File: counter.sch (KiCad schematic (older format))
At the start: 5 parts

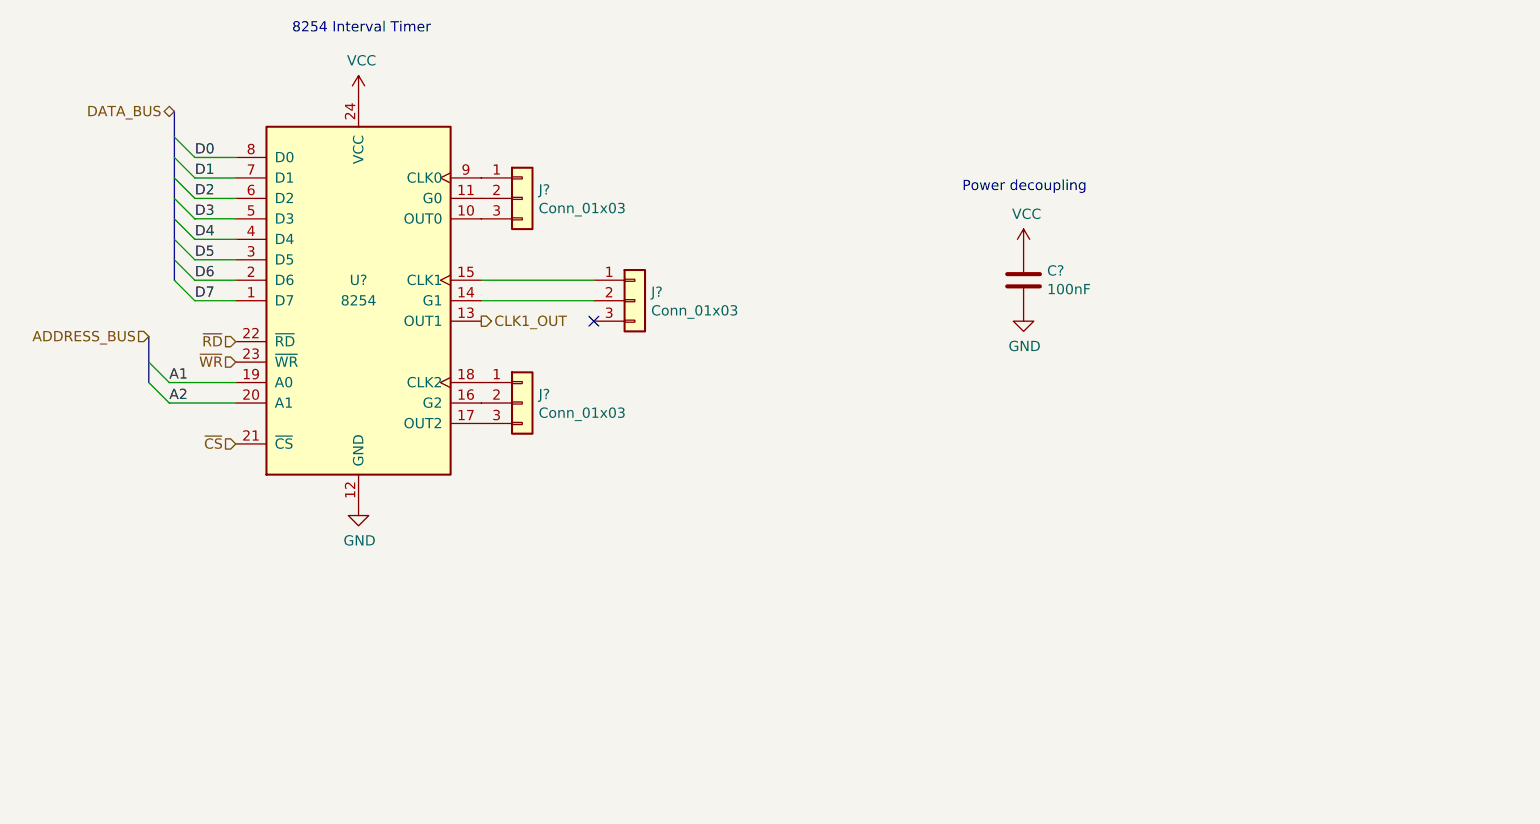
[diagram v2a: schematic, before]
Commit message: General edits; removed floating inputs
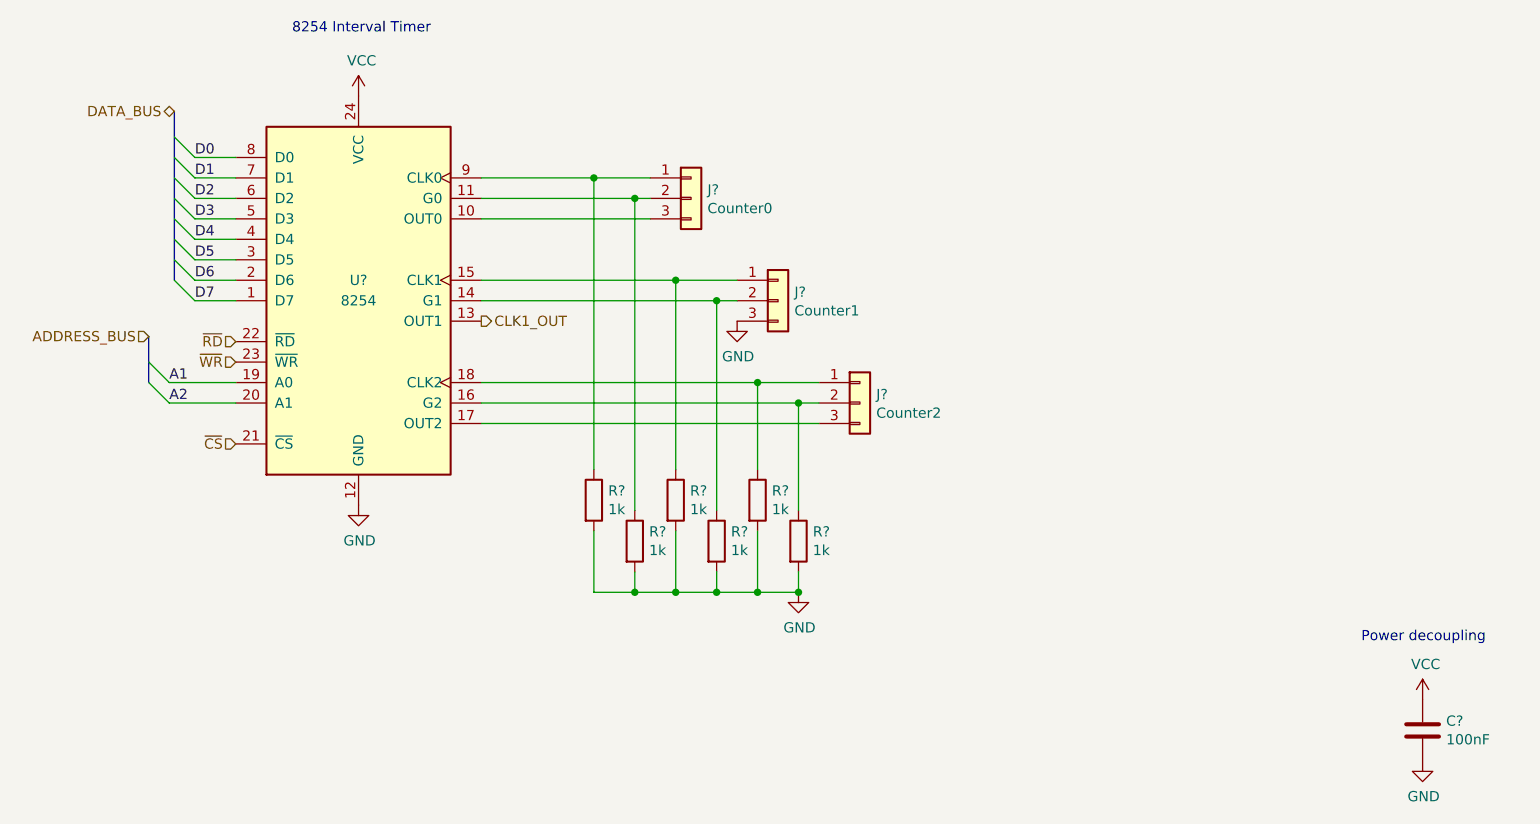
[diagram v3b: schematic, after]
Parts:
- added R? (x6): 1k, symbol Device:R
- J?: value Conn_01x03 -> Counter0
- J?: value Conn_01x03 -> Counter1
- J?: value Conn_01x03 -> Counter2
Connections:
- net GND: now also J?.3 (Pin_3), R?.2, R?.2, R?.2, R?.2, R?.2, R?.2
- net at J?.2 (Pin_2), U?.11 (G0): now also R?.1
- net at J?.2 (Pin_2), U?.14 (G1): now also R?.1
- net at J?.1 (Pin_1), U?.15 (CLK1): now also R?.1
- net at J?.2 (Pin_2), U?.16 (G2): now also R?.1
- net at J?.1 (Pin_1), U?.18 (CLK2): now also R?.1
- net at J?.1 (Pin_1), U?.9 (CLK0): now also R?.1
- no-connect marks 1 -> 0
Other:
- moved on the sheet: C?, J?

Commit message: Updates to pass ERC
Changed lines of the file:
@@
 D7
 Text HLabel 4100 2800 0    50   BiDi ~ 0
-DATA_BUS
+D[0..15]
 Text HLabel 4400 3925 0    50   Input ~ 0
 ~RD
@@
 	3975 4125 4075 4225
 Text HLabel 3975 3900 0    50   Input ~ 0
-ADDRESS_BUS
+A[0..19]
 Text HLabel 4400 4425 0    50   Input ~ 0
 ~CS
@@
 Wire Wire Line
 	6150 5150 6350 5150
-Wire Bus Line
-	3975 3900 3975 4125
-Wire Bus Line
-	4100 2800 4100 3625
 Connection ~ 6350 5150
 $Comp
@@
 	1    0    0    -1
 $EndComp
+Wire Bus Line
+	3975 3900 3975 4125
+Wire Bus Line
+	4100 2800 4100 3625
 $EndSCHEMATC

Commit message: Assign footprints for most symbols
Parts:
- C20: renamed from C?; footprint (none) -> Capacitor_THT:C_Rect_L4.0mm_W2.5mm_P2.50mm
- J17, J18, J19: renamed from J?; footprint (none) -> Connector_PinHeader_2.54mm:PinHeader_1x03_P2.54mm_Vertical
- R12, R13, R14, R15, R16, R17: renamed from R?; footprint (none) -> Resistor_THT:R_Axial_DIN0207_L6.3mm_D2.5mm_P10.16mm_Horizontal
- gave numbers to parts that had none: 1
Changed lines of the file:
@@
 $EndDescr
 $Comp
-L Timer:8254 U?
+L Timer:8254 U17
 U 1 1 61CE17BA
 P 5000 3725
-F 0 "U?" H 5000 3825 50  0000 C CNN
+F 0 "U17" H 5000 3825 50  0000 C CNN
 F 1 "8254" H 5000 3725 50  0000 C CNN
 F 2 "Package_DIP:DIP-24_W15.24mm" H 5050 3975 50  0001 C CNN
@@
 ~CS
 $Comp
-L Connector_Generic:Conn_01x03 J?
+L Connector_Generic:Conn_01x03 J17
 U 1 1 61CE9805
 P 6625 3225
-F 0 "J?" H 6705 3267 50  0000 L CNN
+F 0 "J17" H 6705 3267 50  0000 L CNN
 F 1 "Counter0" H 6705 3176 50  0000 L CNN
-F 2 "" H 6625 3225 50  0001 C CNN
+F 2 "Connector_PinHeader_2.54mm:PinHeader_1x03_P2.54mm_Vertical" H 6625 3225 50  0001 C CNN
 F 3 "~" H 6625 3225 50  0001 C CNN
 	1    6625 3225
@@
 $EndComp
 $Comp
-L Connector_Generic:Conn_01x03 J?
+L Connector_Generic:Conn_01x03 J18
 U 1 1 61CE9E55
 P 7050 3725
-F 0 "J?" H 7130 3767 50  0000 L CNN
+F 0 "J18" H 7130 3767 50  0000 L CNN
 F 1 "Counter1" H 7130 3676 50  0000 L CNN
-F 2 "" H 7050 3725 50  0001 C CNN
+F 2 "Connector_PinHeader_2.54mm:PinHeader_1x03_P2.54mm_Vertical" H 7050 3725 50  0001 C CNN
 F 3 "~" H 7050 3725 50  0001 C CNN
 	1    7050 3725
@@
 $EndComp
 $Comp
-L Connector_Generic:Conn_01x03 J?
+L Connector_Generic:Conn_01x03 J19
 U 1 1 61CEA43A
 P 7450 4225
-F 0 "J?" H 7530 4267 50  0000 L CNN
+F 0 "J19" H 7530 4267 50  0000 L CNN
 F 1 "Counter2" H 7530 4176 50  0000 L CNN
-F 2 "" H 7450 4225 50  0001 C CNN
+F 2 "Connector_PinHeader_2.54mm:PinHeader_1x03_P2.54mm_Vertical" H 7450 4225 50  0001 C CNN
 F 3 "~" H 7450 4225 50  0001 C CNN
 	1    7450 4225
@@
 CLK1_OUT
 $Comp
-L power:VCC #PWR?
+L power:VCC #PWR0170
 U 1 1 61CEF955
 P 5000 2725
-F 0 "#PWR?" H 5000 2575 50  0001 C CNN
+F 0 "#PWR0170" H 5000 2575 50  0001 C CNN
 F 1 "VCC" H 5015 2898 50  0000 C CNN
 F 2 "" H 5000 2725 50  0001 C CNN
@@
 $EndComp
 $Comp
-L power:GND #PWR?
+L power:GND #PWR0171
 U 1 1 61CEFD63
 P 5000 4725
-F 0 "#PWR?" H 5000 4475 50  0001 C CNN
+F 0 "#PWR0171" H 5000 4475 50  0001 C CNN
 F 1 "GND" H 5005 4552 50  0000 C CNN
 F 2 "" H 5000 4725 50  0001 C CNN
@@
 $EndComp
 $Comp
-L Device:C C?
+L Device:C C20
 U 1 1 61CF103C
 P 10200 5825
-F 0 "C?" H 10315 5871 50  0000 L CNN
+F 0 "C20" H 10315 5871 50  0000 L CNN
 F 1 "100nF" H 10315 5780 50  0000 L CNN
-F 2 "" H 10238 5675 50  0001 C CNN
+F 2 "Capacitor_THT:C_Rect_L4.0mm_W2.5mm_P2.50mm" H 10238 5675 50  0001 C CNN
 F 3 "~" H 10200 5825 50  0001 C CNN
 	1    10200 5825
@@
 $EndComp
 $Comp
-L power:VCC #PWR?
+L power:VCC #PWR0172
 U 1 1 61CF1476
 P 10200 5675
-F 0 "#PWR?" H 10200 5525 50  0001 C CNN
+F 0 "#PWR0172" H 10200 5525 50  0001 C CNN
 F 1 "VCC" H 10215 5848 50  0000 C CNN
 F 2 "" H 10200 5675 50  0001 C CNN
@@
 $EndComp
 $Comp
-L power:GND #PWR?
+L power:GND #PWR0173
 U 1 1 61CF1948
 P 10200 5975
-F 0 "#PWR?" H 10200 5725 50  0001 C CNN
+F 0 "#PWR0173" H 10200 5725 50  0001 C CNN
 F 1 "GND" H 10205 5802 50  0000 C CNN
 F 2 "" H 10200 5975 50  0001 C CNN
@@
 	5600 4325 7250 4325
 $Comp
-L Device:R R?
+L Device:R R12
 U 1 1 622F8E00
 P 6150 4700
-F 0 "R?" H 6220 4746 50  0000 L CNN
+F 0 "R12" H 6220 4746 50  0000 L CNN
 F 1 "1k" H 6220 4655 50  0000 L CNN
-F 2 "" V 6080 4700 50  0001 C CNN
+F 2 "Resistor_THT:R_Axial_DIN0207_L6.3mm_D2.5mm_P10.16mm_Horizontal" V 6080 4700 50  0001 C CNN
 F 3 "~" H 6150 4700 50  0001 C CNN
 	1    6150 4700
@@
 $EndComp
 $Comp
-L Device:R R?
+L Device:R R13
 U 1 1 622FACCC
 P 6350 4900
-F 0 "R?" H 6420 4946 50  0000 L CNN
+F 0 "R13" H 6420 4946 50  0000 L CNN
 F 1 "1k" H 6420 4855 50  0000 L CNN
-F 2 "" V 6280 4900 50  0001 C CNN
+F 2 "Resistor_THT:R_Axial_DIN0207_L6.3mm_D2.5mm_P10.16mm_Horizontal" V 6280 4900 50  0001 C CNN
 F 3 "~" H 6350 4900 50  0001 C CNN
 	1    6350 4900
@@
 $EndComp
 $Comp
-L Device:R R?
+L Device:R R14
 U 1 1 622FBCA0
 P 6550 4700
-F 0 "R?" H 6620 4746 50  0000 L CNN
+F 0 "R14" H 6620 4746 50  0000 L CNN
 F 1 "1k" H 6620 4655 50  0000 L CNN
-F 2 "" V 6480 4700 50  0001 C CNN
+F 2 "Resistor_THT:R_Axial_DIN0207_L6.3mm_D2.5mm_P10.16mm_Horizontal" V 6480 4700 50  0001 C CNN
 F 3 "~" H 6550 4700 50  0001 C CNN
 	1    6550 4700
@@
 $EndComp
 $Comp
-L Device:R R?
+L Device:R R15
 U 1 1 622FC929
 P 6750 4900
-F 0 "R?" H 6820 4946 50  0000 L CNN
+F 0 "R15" H 6820 4946 50  0000 L CNN
 F 1 "1k" H 6820 4855 50  0000 L CNN
-F 2 "" V 6680 4900 50  0001 C CNN
+F 2 "Resistor_THT:R_Axial_DIN0207_L6.3mm_D2.5mm_P10.16mm_Horizontal" V 6680 4900 50  0001 C CNN
 F 3 "~" H 6750 4900 50  0001 C CNN
 	1    6750 4900
@@
 $EndComp
 $Comp
-L Device:R R?
+L Device:R R16
 U 1 1 622FD532
 P 6950 4700
-F 0 "R?" H 7020 4746 50  0000 L CNN
+F 0 "R16" H 7020 4746 50  0000 L CNN
 F 1 "1k" H 7020 4655 50  0000 L CNN
-F 2 "" V 6880 4700 50  0001 C CNN
+F 2 "Resistor_THT:R_Axial_DIN0207_L6.3mm_D2.5mm_P10.16mm_Horizontal" V 6880 4700 50  0001 C CNN
 F 3 "~" H 6950 4700 50  0001 C CNN
 	1    6950 4700
@@
 $EndComp
 $Comp
-L Device:R R?
+L Device:R R17
 U 1 1 622FE1B8
 P 7150 4900
-F 0 "R?" H 7220 4946 50  0000 L CNN
+F 0 "R17" H 7220 4946 50  0000 L CNN
 F 1 "1k" H 7220 4855 50  0000 L CNN
-F 2 "" V 7080 4900 50  0001 C CNN
+F 2 "Resistor_THT:R_Axial_DIN0207_L6.3mm_D2.5mm_P10.16mm_Horizontal" V 7080 4900 50  0001 C CNN
 F 3 "~" H 7150 4900 50  0001 C CNN
 	1    7150 4900
@@
 Connection ~ 6350 5150
 $Comp
-L power:GND #PWR?
+L power:GND #PWR0174
 U 1 1 6232331C
 P 7150 5150
-F 0 "#PWR?" H 7150 4900 50  0001 C CNN
+F 0 "#PWR0174" H 7150 4900 50  0001 C CNN
 F 1 "GND" H 7155 4977 50  0000 C CNN
 F 2 "" H 7150 5150 50  0001 C CNN
@@
 Connection ~ 7150 5150
 $Comp
-L power:GND #PWR?
+L power:GND #PWR0175
 U 1 1 62324135
 P 6850 3825
-F 0 "#PWR?" H 6850 3575 50  0001 C CNN
+F 0 "#PWR0175" H 6850 3575 50  0001 C CNN
 F 1 "GND" H 6855 3652 50  0000 C CNN
 F 2 "" H 6850 3825 50  0001 C CNN
